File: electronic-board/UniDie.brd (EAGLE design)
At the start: 79.6 x 82.8 mm, 24 parts, among them IC1 ATMEGA88-THIN

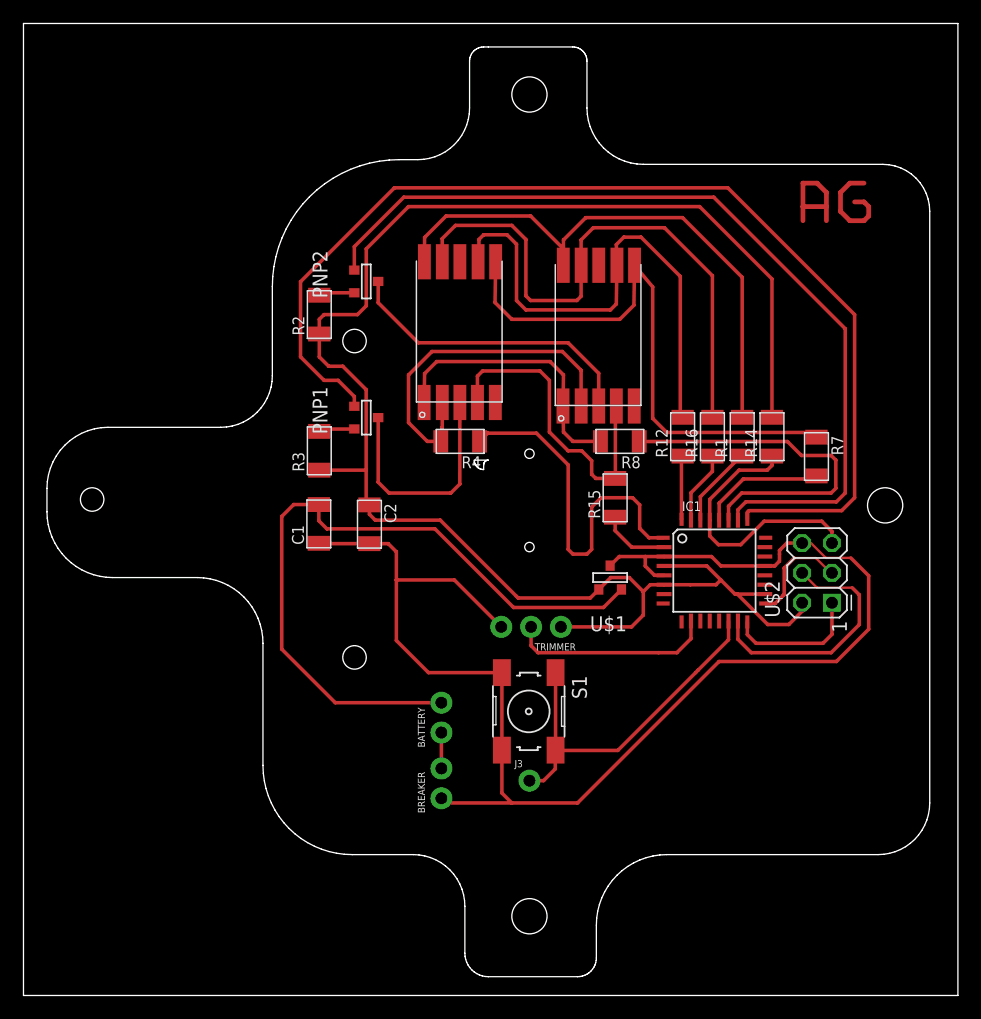
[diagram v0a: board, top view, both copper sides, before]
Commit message: Revert "Adapted parts and routes for milling. Prepared milling files"
This reverts commit d229ee454f50b57581f4fd08392e80f763665f52.
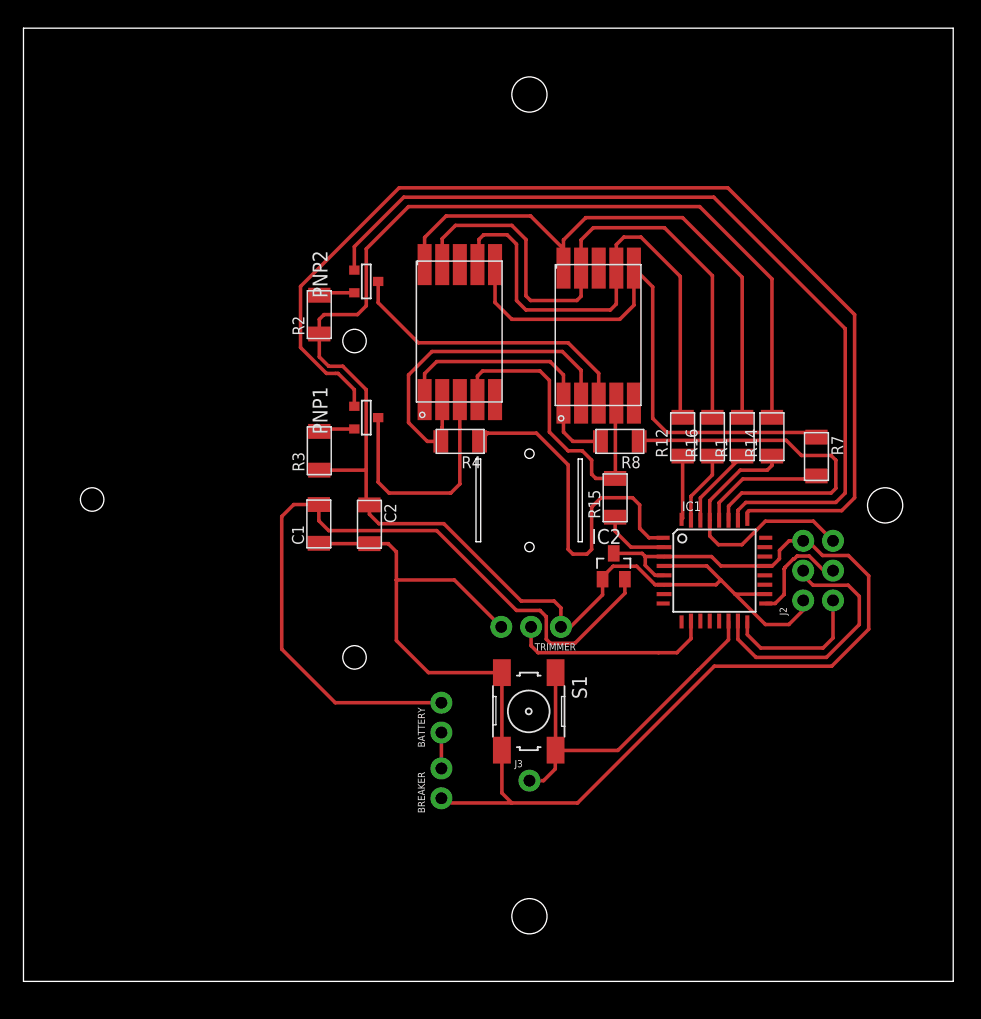
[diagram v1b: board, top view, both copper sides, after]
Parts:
- removed U$1: 5V-REG, AG:SOT-23
- removed U$2: AVRISP, fab:2X03
- added IC2: (no value), fab:SOT23
- added J2: AVR_SPI_PROG_3X2NS, SparkFun-Connectors:2X3-NS
- 7-SEG-LED1, 7-SEG-LED2: value LDS-SMHTA304RISITR -> (none)
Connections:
- net 5V: now also IC2.1, J2.2; no longer U$1.3, U$2.2
- net GND: now also IC2.3, J2.6; no longer U$1.1, U$2.6
- net MISO: now also J2.1; no longer U$2.1
- net MOSI: now also J2.4; no longer U$2.4
- net N$1: now also IC2.2; no longer U$1.2
- net RST: now also J2.5; no longer U$2.5
- net SCK: now also J2.3; no longer U$2.3
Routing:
- net N$11: track 9.93 -> 0.00 mm
- net N$12: track 8.99 -> 0.00 mm
- net N$1: track 61.2 -> 66.2 mm
- net 5V: track 144.1 -> 139.3 mm
- net MISO: track 11.6 -> 12.4 mm
- net SEG10: track 49.4 -> 50.1 mm
- net SEG6: track 48.2 -> 47.6 mm
- net RST: track 23.3 -> 22.7 mm
- net GND: track 121.8 -> 121.3 mm
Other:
- board size 79.6 x 82.8 mm -> 79.2 x 81.2 mm
